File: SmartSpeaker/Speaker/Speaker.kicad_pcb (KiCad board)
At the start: 2 copper layers, 90.7 x 82 mm, 35 parts, among them J102 Screw_Terminal_01x03, J103 Screw_Terminal_01x02, J3 54-00166, Q1 DMG2305UX-13, U1 LM384, U2 LTC1655LCN8, U3 LM2675N-5, U4 LM4040LP-3

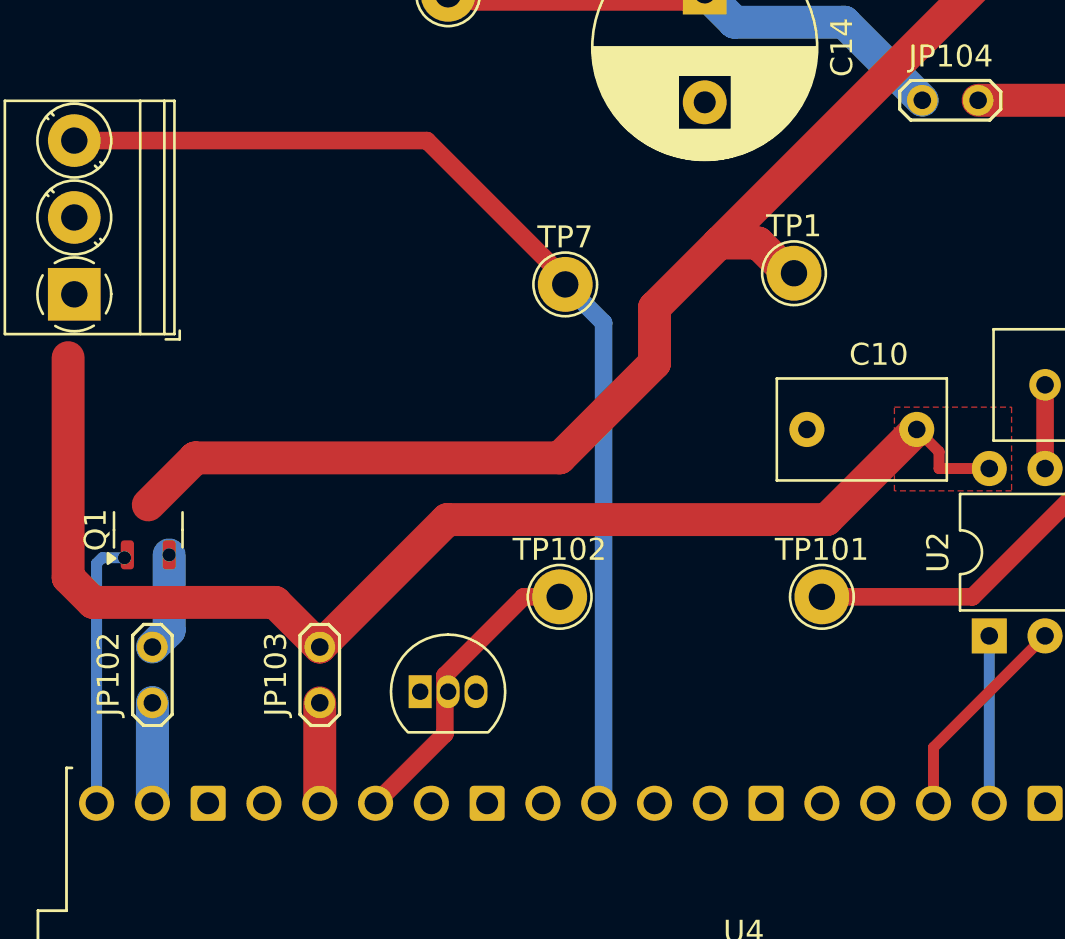
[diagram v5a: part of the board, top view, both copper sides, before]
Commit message: remove bottleneck in ground plane
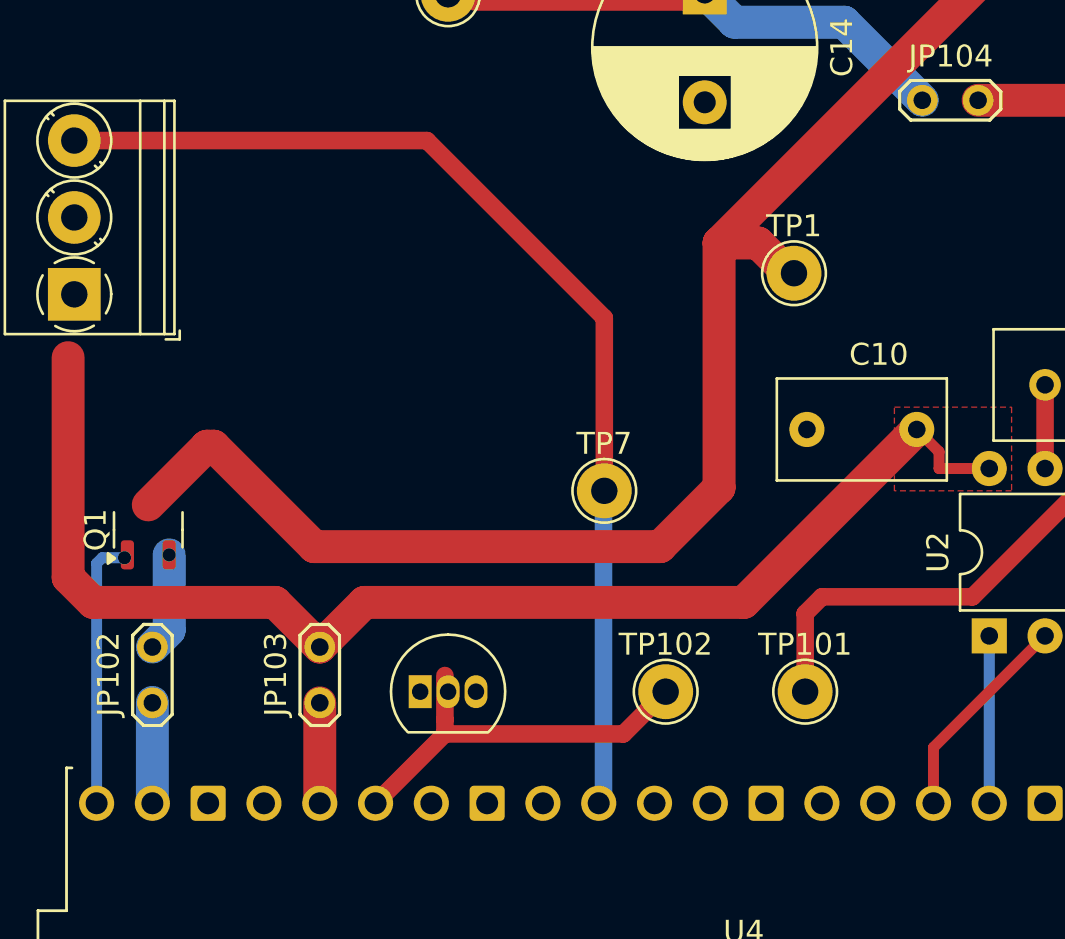
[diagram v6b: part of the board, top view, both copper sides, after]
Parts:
- moved TP7 9.56 mm to (77.0, 72.9)
- moved TP102 6.48 mm to (79.8, 82.0)
- moved TP101 4.38 mm to (86.1, 82.0)
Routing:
- net /Power_converter/5VOut: track 104.1 -> 112.9 mm
- net Net-(A1-ADC_VREF): track 13.8 -> 18.0 mm
- net Net-(U2-REF): track 15.8 -> 19.8 mm
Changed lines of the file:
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@@
 	(footprint "TestPoint:TestPoint_THTPad_D2.5mm_Drill1.2mm"
 		(layer "F.Cu")
-		(at 86.868 77.724)
+		(at 86.106 82.042)
 		(descr "THT pad as test Point, diameter 2.5mm, hole diameter 1.2mm ")
 		(tags "test point THT pad")
@@
 	(footprint "TestPoint:TestPoint_THTPad_D2.5mm_Drill1.2mm"
 		(layer "F.Cu")
-		(at 75.184 63.5)
+		(at 76.962 72.898)
 		(descr "THT pad as test Point, diameter 2.5mm, hole diameter 1.2mm ")
 		(tags "test point THT pad")
@@
 	(footprint "TestPoint:TestPoint_THTPad_D2.5mm_Drill1.2mm"
 		(layer "F.Cu")
-		(at 74.93 77.724)
+		(at 79.756 82.042)
 		(descr "THT pad as test Point, diameter 2.5mm, hole diameter 1.2mm ")
 		(tags "test point THT pad")
@@
 	)
 	(segment
-		(start 73.287 77.724)
-		(end 69.705 81.306)
+		(start 69.705 81.306)
+		(end 69.705 83.312)
 		(width 0.8)
 		(layer "F.Cu")
@@
 	)
 	(segment
-		(start 74.93 77.724)
-		(end 73.287 77.724)
+		(start 69.705 83.312)
+		(end 69.705 83.965)
 		(width 0.8)
 		(layer "F.Cu")
@@
 	)
 	(segment
-		(start 69.705 81.306)
-		(end 69.705 83.965)
+		(start 69.705 83.965)
+		(end 77.833 83.965)
+		(width 0.8)
+		(layer "F.Cu")
+		(net 12)
+	)
+	(segment
+		(start 77.833 83.965)
+		(end 79.756 82.042)
 		(width 0.8)
 		(layer "F.Cu")
@@
 	)
 	(segment
-		(start 75.184 63.246)
-		(end 75.184 63.5)
+		(start 68.89 56.952)
+		(end 76.962 65.024)
 		(width 0.8)
 		(layer "F.Cu")
@@
 	)
 	(segment
-		(start 68.89 56.952)
-		(end 75.184 63.246)
+		(start 52.832 56.952)
+		(end 68.89 56.952)
 		(width 0.8)
 		(layer "F.Cu")
@@
 	)
 	(segment
-		(start 52.832 56.952)
-		(end 68.89 56.952)
+		(start 76.962 65.024)
+		(end 76.962 72.898)
 		(width 0.8)
 		(layer "F.Cu")
@@
 	)
 	(segment
-		(start 76.708 87.122)
-		(end 76.454 86.868)
-		(width 0.2)
+		(start 76.93 73.184)
+		(end 76.93 86.9)
+		(width 0.8)
 		(layer "B.Cu")
 		(net 31)
@@
 	)
 	(segment
-		(start 76.93 65.246)
-		(end 76.93 86.9)
-		(width 0.8)
+		(start 76.708 87.122)
+		(end 76.454 86.868)
+		(width 0.2)
 		(layer "B.Cu")
 		(net 31)
 	)
 	(segment
-		(start 75.184 63.5)
-		(end 76.93 65.246)
+		(start 76.962 73.152)
+		(end 76.93 73.184)
 		(width 0.8)
 		(layer "B.Cu")
@@
 	)
 	(segment
-		(start 64.008 80.01)
-		(end 69.81 74.208)
-		(width 1.5)
+		(start 91.186 70.104)
+		(end 92.202 71.12)
+		(width 0.5)
 		(layer "F.Cu")
 		(net 38)
 	)
 	(segment
-		(start 91.186 70.104)
-		(end 92.202 71.12)
-		(width 0.5)
+		(start 83.312 77.978)
+		(end 91.186 70.104)
+		(width 1.5)
 		(layer "F.Cu")
 		(net 38)
@@
 	)
 	(segment
-		(start 69.81 74.208)
-		(end 87.082 74.208)
+		(start 66.04 77.978)
+		(end 83.312 77.978)
 		(width 1.5)
 		(layer "F.Cu")
@@
 	)
 	(segment
-		(start 87.082 74.208)
-		(end 91.186 70.104)
+		(start 64.008 80.01)
+		(end 66.04 77.978)
 		(width 1.5)
 		(layer "F.Cu")
@@
 	)
 	(segment
-		(start 103.408 42.418)
-		(end 103.408 28.996)
-		(width 0.5)
+		(start 56.2 73.5385)
+		(end 58.8725 70.866)
+		(width 1.5)
 		(layer "F.Cu")
 		(net 40)
 	)
 	(segment
-		(start 74.93 71.398)
-		(end 79.248 67.08)
-		(width 1.5)
+		(start 103.408 42.418)
+		(end 103.408 28.996)
+		(width 0.5)
 		(layer "F.Cu")
 		(net 40)
@@
 	)
 	(segment
-		(start 83.965141 61.613141)
-		(end 82.187141 61.613141)
+		(start 63.754 75.438)
+		(end 79.502 75.438)
 		(width 1.5)
 		(layer "F.Cu")
@@
 	)
 	(segment
-		(start 79.248 67.08)
-		(end 79.248 64.552283)
+		(start 83.965141 61.613141)
+		(end 82.187141 61.613141)
 		(width 1.5)
 		(layer "F.Cu")
@@
 	)
 	(segment
+		(start 58.8725 70.866)
+		(end 59.182 70.866)
+		(width 1.5)
+		(layer "F.Cu")
+		(net 40)
+	)
+	(segment
+		(start 59.182 70.866)
+		(end 63.754 75.438)
+		(width 1.5)
+		(layer "F.Cu")
+		(net 40)
+	)
+	(segment
 		(start 103.408 44.958)
 		(end 103.368 44.918)
@@
 	)
 	(segment
-		(start 56.2 73.5385)
-		(end 58.3405 71.398)
+		(start 85.344 62.992)
+		(end 83.965141 61.613141)
 		(width 1.5)
 		(layer "F.Cu")
@@
 	)
 	(segment
-		(start 85.344 62.992)
-		(end 83.965141 61.613141)
+		(start 79.502 75.438)
+		(end 82.187141 72.752859)
 		(width 1.5)
 		(layer "F.Cu")
@@
 	)
 	(segment
-		(start 58.3405 71.398)
-		(end 74.93 71.398)
-		(width 1.5)
-		(layer "F.Cu")
-		(net 40)
-	)
-	(segment
-		(start 79.248 64.552283)
+		(start 82.187141 72.752859)
 		(end 82.187141 61.613141)
 		(width 1.5)
@@
 	)
 	(segment
+		(start 86.106 78.486)
+		(end 86.106 82.042)
+		(width 0.8)
+		(layer "F.Cu")
+		(net 45)
+	)
+	(segment
 		(start 93.726 77.724)
 		(end 99.568 71.882)
@@
 	(segment
 		(start 86.868 77.724)
-		(end 87.376 77.216)
-		(width 0.5)
+		(end 86.106 78.486)
+		(width 0.8)
 		(layer "F.Cu")
 		(net 45)

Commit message: lots of small improvements
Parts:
- added REF**: Polarity_Center_Positive_6mm_SilkScreen, Symbol:Polarity_Center_Positive_6mm_SilkScreen, F.Cu at (69.0, 31.1)
- added TP3: Ground, TestPoint:TestPoint_THTPad_D2.5mm_Drill1.2mm, F.Cu at (107.7, 73.7)
- added TP3: Ground, TestPoint:TestPoint_THTPad_D2.5mm_Drill1.2mm, F.Cu at (118.6, 39.9)
- added TP8: DAC_Out, TestPoint:TestPoint_THTPad_D2.5mm_Drill1.2mm, F.Cu at (95.8, 62.0)
- J1: renamed from J103; value Screw_Terminal_01x02 -> Terminal_2
- J2: renamed from J102; value Screw_Terminal_01x03 -> Terminal_3
- JP1: renamed from JP104; value Jumper_2_Bridged -> Jumper_NC
- JP2: renamed from JP102; value Jumper_2_Bridged -> Jumper_NC
- JP3: renamed from JP103; value Jumper_2_Bridged -> Jumper_NC
- RV1: value R_Potentiometer_Trim -> Trim_Pot
- TP1: value TestPoint -> 5Volts
- TP10: renamed from TP7; value TestPoint -> MicIn
- TP2: value TestPoint -> 24Volts
- TP3: value TestPoint -> Ground
- TP4: value TestPoint -> ON/~{OFF}
- TP5: value TestPoint -> AmpOut
- TP6: value TestPoint -> AmpIn
- TP7: renamed from TP102; value TestPoint -> 3V_Ref
- TP9: renamed from TP101; value TestPoint -> DAC_Ref
- moved TP3 7.38 mm to (61.5, 52.8)
- moved J3 6.08 mm to (63.3, 40.2)
- moved TP4 3.45 mm to (70.4, 39.6)
- moved C6 1.63 mm to (90.6, 71.6)
- renumbered C7 to C1, C3 to C2, C5 to C3, C6 to C5, C10 to C6, U4 to U2, U2 to U4
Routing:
- net Net-(U4-VOUT): track 3.82 -> 12.5 mm
- net Net-(U3-ON/~{OFF}): track 6.43 -> 10.2 mm
- net VDD: track 58.5 -> 62.1 mm
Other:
- board text added: "12-24 Volts In"
- board text added: "24Volts"
- board text added: "3V_Ref"
- board text added: "5V_Reg"
- board text added: "5Volts"
- board text added: "Amp"
- board text added: "AmpIn"
- board text added: "AmpOut"
- board text added: "DAC"
- board text added: "DAC_Out"
- board text added: "DAC_Ref"
- board text added: "Ground"
- board text added: "Inductor"
- board text added: "Mic In"
- board text added: "MicIn"
- board text added: "ON/~{OFF}"
- board text added: "Pi Pico W"
- board text added: "Speaker Out"

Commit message: lots of improvements, many semi-cosmetic
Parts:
- added H1: MountingHole_Pad, MountingHole:MountingHole_3.2mm_M3_Pad, F.Cu at (50.8, 31.8)
- added H2: MountingHole_Pad, MountingHole:MountingHole_3.2mm_M3_Pad, F.Cu at (134.6, 31.8)
- added H3: MountingHole_Pad, MountingHole:MountingHole_3.2mm_M3_Pad, F.Cu at (50.8, 106.7)
- added H4: MountingHole_Pad, MountingHole:MountingHole_3.2mm_M3_Pad, F.Cu at (134.6, 106.7)
- added REF**: KiCad-Logo2_5mm_SilkScreen, Symbol:KiCad-Logo2_5mm_SilkScreen, F.Cu at (113.5, 103.1)
- added REF**: Smolhaj_Scale_0.1, Symbol:Smolhaj_Scale_0.1, F.Cu at (123.6, 98.8)
- added REF**: OSHW-Logo_5.7x6mm_SilkScreen, Symbol:OSHW-Logo_5.7x6mm_SilkScreen, F.Cu at (110.8, 95.5)
- moved TP3 8.77 mm to (63.0, 61.5)
- moved J3 3.69 mm to (60.9, 43.0)
- moved REF** 2.89 mm to (71.9, 31.6)
- moved J2 2.03 mm to (50.8, 64.0)
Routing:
- net /Power_converter/VoltageIn: track 26.4 -> 40.7 mm
- net /Adafruit_1713_Microphone/OUTPUT: track 49.8 -> 51.8 mm
- net VDD: track 62.1 -> 62.7 mm
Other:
- board size 90.7 x 82 mm -> 94 x 85.1 mm
- board text added: "12-24VDC In"
- board text added: "3V Ref"
- board text added: "5V Reg"
- board text added: "DAC Out"
- board text added: "DAC Ref"
- board text removed: "12-24 Volts In"
- board text removed: "3V_Ref"
- board text removed: "5V_Reg"
- board text removed: "DAC_Out"
- board text removed: "DAC_Ref"
- board text removed: "MicIn"
